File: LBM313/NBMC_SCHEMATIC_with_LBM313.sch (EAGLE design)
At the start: 34 parts, among them Q1 32.768kHz, U3 AD8232ACPZ_R7

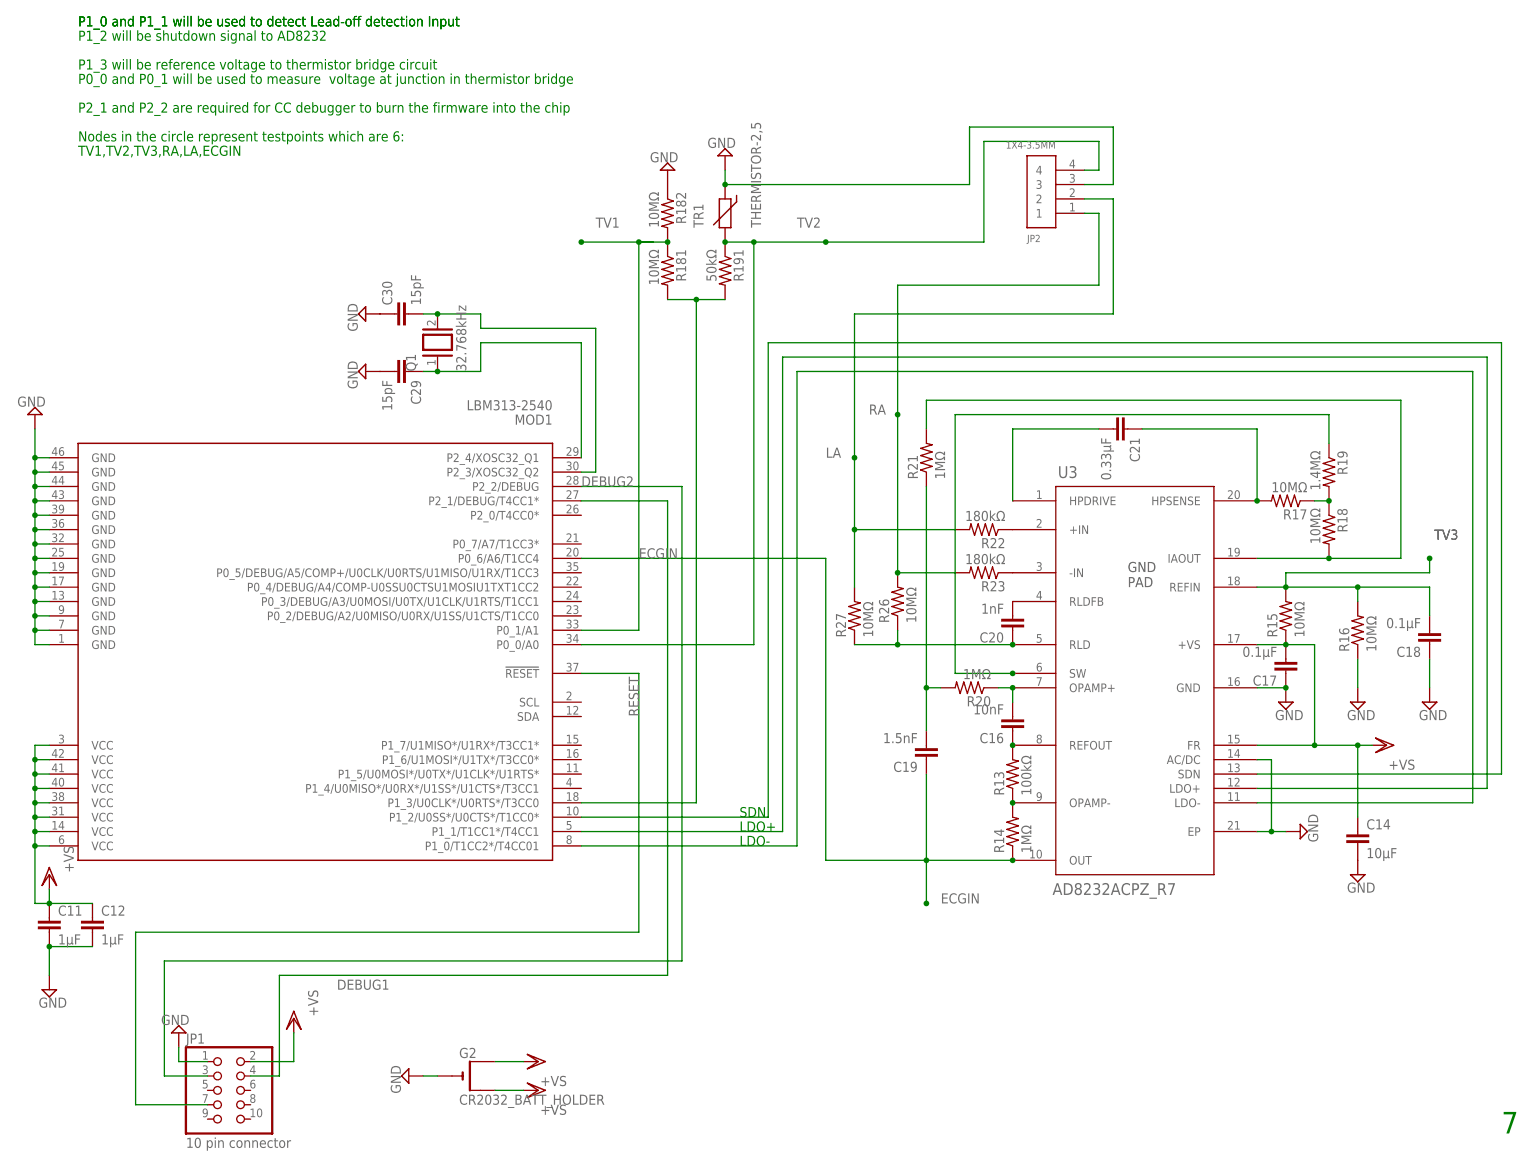
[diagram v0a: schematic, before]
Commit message: added testpoints ,100uf cap, cap across thermistor,JP2,removed battery and battery holder connection proper
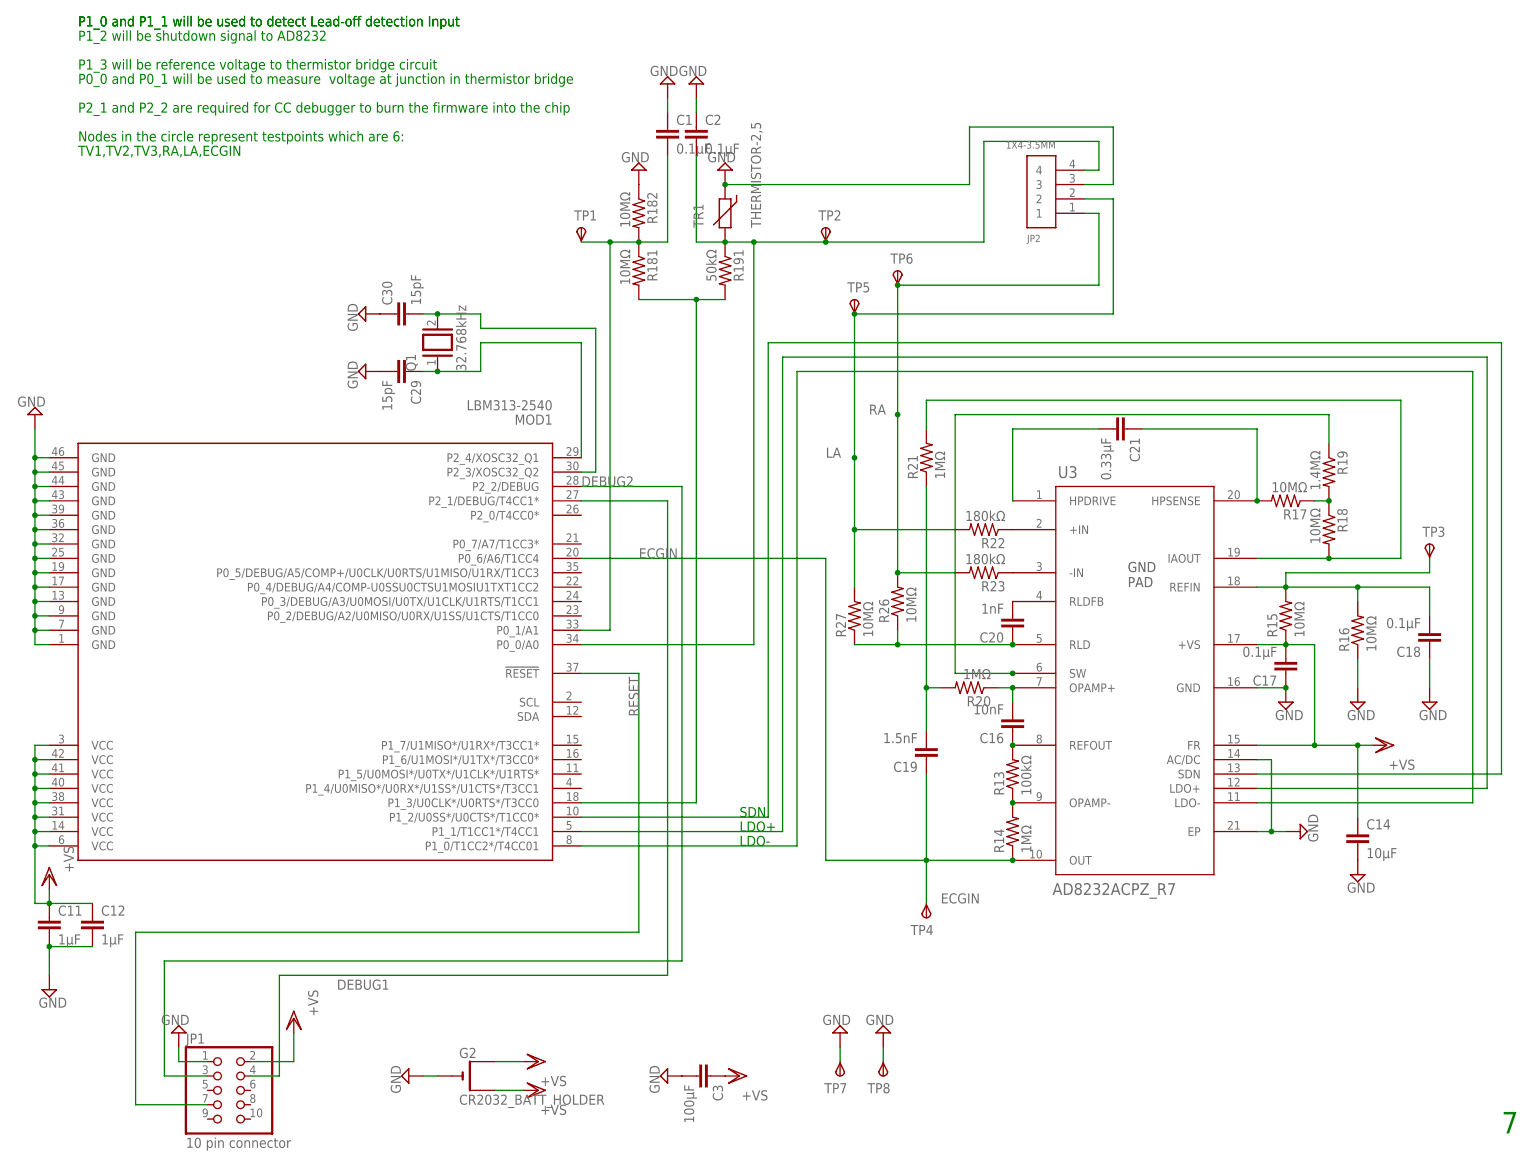
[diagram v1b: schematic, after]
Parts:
- added C1, C2: 0.1µF, rcl:C-EUC0402
- added C3: 100µF, rcl:C-EUC0402
- added TP1, TP2, TP3, TP4, TP5, TP6, TP7, TP8: TPSTP09R, testpad:TPSTP09R
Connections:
- net ECGIN: now also TP4.PP
- net GND: now also C1.1, C2.1, C3.2, TP7.PP, TP8.PP
- net LA: now also TP5.PP
- net RA: now also TP6.PP
- net TV1: now also C1.2, TP1.PP
- net TV2: now also C2.2, TP2.PP
- net TV3: now also TP3.PP
- net VSS: now also C3.1
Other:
- moved on the sheet: R181, R182

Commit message: updated BOM with the new changes of TP,100uF cap etc
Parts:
- renumbered C1 to C181, C2 to C191, C29 to C291, C3 to C31, C30 to C301
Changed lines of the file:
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@@
 <part name="SUPPLY1" library="supply2" deviceset="GND" device=""/>
 <part name="SUPPLY3" library="supply2" deviceset="GND" device=""/>
-<part name="C29" library="rcl" deviceset="C-EU" device="C0402" value="15pF"/>
-<part name="C30" library="rcl" deviceset="C-EU" device="C0402" value="15pF"/>
+<part name="C291" library="rcl" deviceset="C-EU" device="C0402" value="15pF"/>
+<part name="C301" library="rcl" deviceset="C-EU" device="C0402" value="15pF"/>
 <part name="VSS2" library="supply1" deviceset="VSS" device="" value="+VS"/>
 <part name="SUPPLY9" library="supply2" deviceset="GND" device=""/>
@@
 <part name="TP5" library="testpad" deviceset="TPS" device="TP09R"/>
 <part name="TP6" library="testpad" deviceset="TPS" device="TP09R"/>
-<part name="C1" library="rcl" deviceset="C-EU" device="C0402" value="0.1µF"/>
+<part name="C181" library="rcl" deviceset="C-EU" device="C0402" value="0.1µF"/>
 <part name="SUPPLY8" library="supply2" deviceset="GND" device=""/>
-<part name="C2" library="rcl" deviceset="C-EU" device="C0402" value="0.1µF"/>
+<part name="C191" library="rcl" deviceset="C-EU" device="C0402" value="0.1µF"/>
 <part name="SUPPLY15" library="supply2" deviceset="GND" device=""/>
 <part name="TP7" library="testpad" deviceset="TPS" device="TP09R"/>
@@
 <part name="SUPPLY16" library="supply2" deviceset="GND" device=""/>
 <part name="SUPPLY17" library="supply2" deviceset="GND" device=""/>
-<part name="C3" library="rcl" deviceset="C-EU" device="C0402" value="100µF"/>
+<part name="C31" library="rcl" deviceset="C-EU" device="C0402" value="100µF"/>
 <part name="SUPPLY18" library="supply2" deviceset="GND" device=""/>
 <part name="VSS6" library="supply1" deviceset="VSS" device="" value="+VS"/>
@@
 <instance part="SUPPLY1" gate="GND" x="-101.6" y="-66.04"/>
 <instance part="SUPPLY3" gate="GND" x="-104.14" y="35.56" rot="R180"/>
-<instance part="C29" gate="G$1" x="-38.1" y="43.18" rot="R270"/>
-<instance part="C30" gate="G$1" x="-40.64" y="53.34" rot="R90"/>
+<instance part="C291" gate="G$1" x="-38.1" y="43.18" rot="R270"/>
+<instance part="C301" gate="G$1" x="-40.64" y="53.34" rot="R90"/>
 <instance part="VSS2" gate="G$1" x="-58.42" y="-71.12" rot="R180"/>
 <instance part="SUPPLY9" gate="GND" x="-78.74" y="-73.66" rot="R180"/>
@@
 <instance part="TP5" gate="G$1" x="40.64" y="55.88"/>
 <instance part="TP6" gate="G$1" x="48.26" y="60.96"/>
-<instance part="C1" gate="G$1" x="7.62" y="86.36"/>
+<instance part="C181" gate="G$1" x="7.62" y="86.36"/>
 <instance part="SUPPLY8" gate="GND" x="7.62" y="93.98" rot="R180"/>
-<instance part="C2" gate="G$1" x="12.7" y="86.36"/>
+<instance part="C191" gate="G$1" x="12.7" y="86.36"/>
 <instance part="SUPPLY15" gate="GND" x="12.7" y="93.98" rot="R180"/>
 <instance part="TP7" gate="G$1" x="38.1" y="-81.28" rot="R180"/>
@@
 <instance part="SUPPLY16" gate="GND" x="38.1" y="-73.66" rot="R180"/>
 <instance part="SUPPLY17" gate="GND" x="45.72" y="-73.66" rot="R180"/>
-<instance part="C3" gate="G$1" x="15.24" y="-81.28" rot="R270"/>
+<instance part="C31" gate="G$1" x="15.24" y="-81.28" rot="R270"/>
 <instance part="SUPPLY18" gate="GND" x="7.62" y="-81.28" rot="R270"/>
 <instance part="VSS6" gate="G$1" x="20.32" y="-81.28" rot="R90"/>
@@
 </segment>
 <segment>
-<pinref part="C29" gate="G$1" pin="2"/>
+<pinref part="C291" gate="G$1" pin="2"/>
 <pinref part="SUPPLY6" gate="GND" pin="GND"/>
 </segment>
 <segment>
-<pinref part="C30" gate="G$1" pin="1"/>
+<pinref part="C301" gate="G$1" pin="1"/>
 <pinref part="SUPPLY7" gate="GND" pin="GND"/>
 </segment>
@@
 </segment>
 <segment>
-<pinref part="C1" gate="G$1" pin="1"/>
+<pinref part="C181" gate="G$1" pin="1"/>
 <pinref part="SUPPLY8" gate="GND" pin="GND"/>
 <wire x1="7.62" y1="88.9" x2="7.62" y2="91.44" width="0.1524" layer="91"/>
 </segment>
 <segment>
-<pinref part="C2" gate="G$1" pin="1"/>
+<pinref part="C191" gate="G$1" pin="1"/>
 <pinref part="SUPPLY15" gate="GND" pin="GND"/>
 <wire x1="12.7" y1="88.9" x2="12.7" y2="91.44" width="0.1524" layer="91"/>
@@
 </segment>
 <segment>
-<pinref part="C3" gate="G$1" pin="2"/>
+<pinref part="C31" gate="G$1" pin="2"/>
 <pinref part="SUPPLY18" gate="GND" pin="GND"/>
 </segment>
@@
 </segment>
 <segment>
-<pinref part="C3" gate="G$1" pin="1"/>
+<pinref part="C31" gate="G$1" pin="1"/>
 <pinref part="VSS6" gate="G$1" pin="VSS"/>
 </segment>
@@
 <pinref part="TP2" gate="G$1" pin="PP"/>
 <junction x="35.56" y="66.04"/>
-<pinref part="C2" gate="G$1" pin="2"/>
+<pinref part="C191" gate="G$1" pin="2"/>
 <wire x1="12.7" y1="81.28" x2="12.7" y2="66.04" width="0.1524" layer="91"/>
 <wire x1="12.7" y1="66.04" x2="17.78" y2="66.04" width="0.1524" layer="91"/>
@@
 <segment>
 <wire x1="-25.4" y1="48.26" x2="-25.4" y2="43.18" width="0.1524" layer="91"/>
-<pinref part="C29" gate="G$1" pin="1"/>
+<pinref part="C291" gate="G$1" pin="1"/>
 <wire x1="-25.4" y1="43.18" x2="-33.02" y2="43.18" width="0.1524" layer="91"/>
 <wire x1="-33.02" y1="43.18" x2="-35.56" y2="43.18" width="0.1524" layer="91"/>
@@
 <wire x1="-33.02" y1="53.34" x2="-35.56" y2="53.34" width="0.1524" layer="91"/>
 <junction x="-33.02" y="53.34"/>
-<pinref part="C30" gate="G$1" pin="2"/>
+<pinref part="C301" gate="G$1" pin="2"/>
 <pinref part="Q1" gate="G$1" pin="2"/>
 <wire x1="-25.4" y1="50.8" x2="-5.08" y2="50.8" width="0.1524" layer="91"/>
@@
 <junction x="-2.54" y="66.04"/>
 <pinref part="TP1" gate="G$1" pin="PP"/>
-<pinref part="C1" gate="G$1" pin="2"/>
+<pinref part="C181" gate="G$1" pin="2"/>
 <wire x1="2.54" y1="66.04" x2="7.62" y2="66.04" width="0.1524" layer="91"/>
 <wire x1="7.62" y1="66.04" x2="7.62" y2="81.28" width="0.1524" layer="91"/>

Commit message: reset filter is added, Thermistor removed and the testpoint connections to the JP1 are removed
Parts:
- removed C291: 15pF, rcl:C-EUC0402
- removed TR1: THERMISTOR-2,5, varistor:THERMISTOR-2,5
- added C29: 15pF, rcl:C-EUC0402
- added C32: 1nF, rcl:C-EUC0402
- added R28: 4.7kΩ, rcl:R-US_R0402
- C31: device rcl:C-EUC0402 -> resistor:C-EUC1210
- renumbered C301 to C30
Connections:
- new net RESET_FILT: C32.1, MOD1.!RESET!, R28.1
- net ECGIN: now also TP6.PP; no longer TP4.PP
- net GND: now also C29.1, C32.2, JP2.4; no longer C291.2, JP2.3, TR1.1
- net LA: now also JP2.1, TP4.PP; no longer JP2.2, TP5.PP
- net N$23: now also MOD1.P1_3/U0CLK*/U0RTS*/T3CC0
- net RA: now also JP2.2, TP5.PP; no longer JP2.1, TP6.PP
- net RESET: now also R28.2; no longer MOD1.!RESET!
- net TV2: now also JP2.3; no longer JP2.4, TR1.2
- net VSS1: now also C29.2; no longer C291.1
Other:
- note added: "8"
- note added: "Six Testpoints are represented as TP1-TP6"
- note removed: "7"
- note removed: "Nodes in the circle represent testpoints which are 6:"
- note removed: "TV1,TV2,TV3,RA,LA,ECGIN"
- moved on the sheet: TP4, TP5, TP6

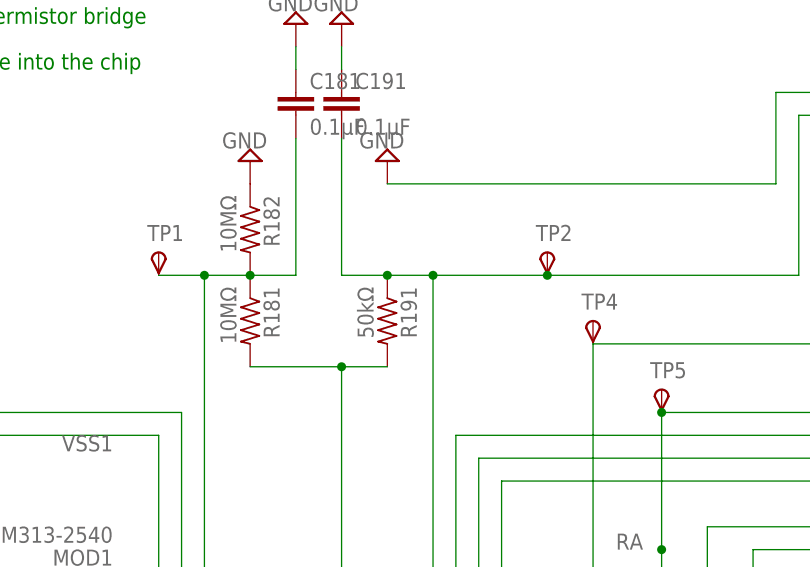
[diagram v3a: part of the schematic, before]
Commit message: mouser BOM added and ordered
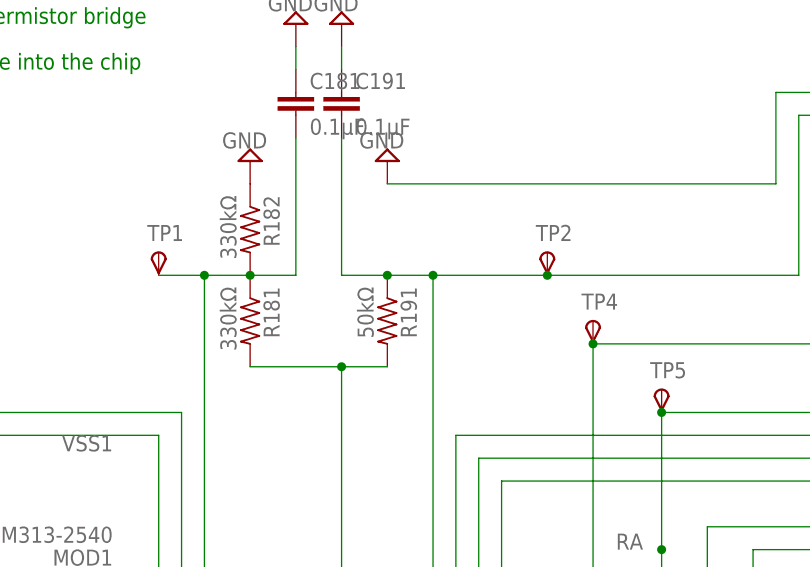
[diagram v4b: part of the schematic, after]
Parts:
- R181, R182: value 10MΩ -> 330kΩ
- R20: value 1MΩ -> 1MΩ
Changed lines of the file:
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@@
 <part name="R18" library="rcl" deviceset="R-US_" device="R0402" value="10MΩ"/>
 <part name="R19" library="rcl" deviceset="R-US_" device="R0402" value="1.4MΩ"/>
-<part name="R20" library="rcl" deviceset="R-US_" device="R0402" value="1MΩ "/>
+<part name="R20" library="rcl" deviceset="R-US_" device="R0402" value="1MΩ"/>
 <part name="R21" library="rcl" deviceset="R-US_" device="R0402" value="1MΩ"/>
 <part name="C19" library="rcl" deviceset="C-EU" device="C0402" value="1.5nF"/>
@@
 <part name="C14" library="rcl" deviceset="C-EU" device="C0402" value="10µF"/>
 <part name="SUPPLY14" library="supply2" deviceset="GND" device=""/>
-<part name="R181" library="rcl" deviceset="R-US_" device="R0402" value="10MΩ"/>
-<part name="R182" library="rcl" deviceset="R-US_" device="R0402" value="10MΩ"/>
+<part name="R181" library="rcl" deviceset="R-US_" device="R0402" value="330kΩ"/>
+<part name="R182" library="rcl" deviceset="R-US_" device="R0402" value="330kΩ"/>
 <part name="SUPPLY4" library="supply2" deviceset="GND" device=""/>
 <part name="MOD1" library="LBM313-2540" deviceset="LBM313-2540" device=""/>
@@
 <part name="TP3" library="testpad" deviceset="TPS" device="TP09R"/>
 <part name="TP6" library="testpad" deviceset="TPS" device="TP09R"/>
-<part name="TP4" library="testpad" deviceset="TPS" device="TP09R"/>
 <part name="TP5" library="testpad" deviceset="TPS" device="TP09R"/>
 <part name="C181" library="rcl" deviceset="C-EU" device="C0402" value="0.1µF"/>
@@
 <part name="C32" library="rcl" deviceset="C-EU" device="C0402" value="1nF"/>
 <part name="SUPPLY19" library="supply2" deviceset="GND" device=""/>
+<part name="TP4" library="testpad" deviceset="TPS" device="TP09R"/>
 </parts>
 <sheets>
@@
 <instance part="TP3" gate="G$1" x="142.24" y="12.7"/>
 <instance part="TP6" gate="G$1" x="53.34" y="-53.34" rot="R180"/>
-<instance part="TP4" gate="G$1" x="40.64" y="60.96"/>
 <instance part="TP5" gate="G$1" x="48.26" y="53.34"/>
 <instance part="C181" gate="G$1" x="7.62" y="86.36"/>
@@
 <instance part="C32" gate="G$1" x="-5.08" y="-53.34" rot="R180"/>
 <instance part="SUPPLY19" gate="GND" x="-5.08" y="-45.72" rot="R180"/>
+<instance part="TP4" gate="G$1" x="40.64" y="60.96"/>
 </instances>
 <busses>
@@
 <wire x1="40.64" y1="27.94" x2="40.64" y2="58.42" width="0.1524" layer="91"/>
 <junction x="40.64" y="27.94"/>
-<pinref part="TP4" gate="G$1" pin="PP"/>
 <pinref part="JP2" gate="G$1" pin="1"/>
 <wire x1="83.82" y1="71.12" x2="81.28" y2="71.12" width="0.1524" layer="91"/>
 <wire x1="83.82" y1="58.42" x2="83.82" y2="71.12" width="0.1524" layer="91"/>
 <wire x1="83.82" y1="58.42" x2="40.64" y2="58.42" width="0.1524" layer="91"/>
-</segment>
-</net>
+<pinref part="TP4" gate="G$1" pin="PP"/>
+<junction x="40.64" y="58.42"/>
+</segment>
+</net>
